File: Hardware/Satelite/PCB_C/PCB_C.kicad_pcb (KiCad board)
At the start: 2 copper layers, 54 x 54 mm, 50 parts, among them IC1 MCP1501T-33E_CHY, IC2 IS25LP080D-JULE-TR, IC3 BQ24392RSER, IC4 MS563702BA03-50, IC5 BMX055, J1 Conn_01x06, J2 JUMPER, J3 Conector_PCB_B-C, J4 Conector_Expansion_CanSat, J5 USB_B_Micro, Q1 BC817, U1 NTB0104BQ,115, U2 TCA9802DGKR, U3 STM32F303RETx, U4 NTB0104BQ,115, U5 SN74LVC1G3157DCKR, U6 Si7006-A20-IM1, Y1 LFXTAL016178, Y2 Crystal

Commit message: PCB C actualizado con nuevo conector (WIP)
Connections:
- J3 pad 1: +BATT -> GND
- J3 pad 10: /I_SENSE_3V3 -> +3V3_Internal
- J3 pad 11: /V_SENSE_3V3 -> /V_SENSE_5V
- J3 pad 12: /V_SENSE_5V -> /I_SENSE_5V
- J3 pad 13: GND -> +5V
- J3 pad 14: +5V -> /5V_ENABLE
- J3 pad 15: GND -> /V_SENSE_3V3
- J3 pad 16: GND -> /I_SENSE_3V3
- J3 pad 17: +3V3_Internal -> +3V3
- J3 pad 18: +3V3 -> /3V_ENABLE
- J3 pad 19: +BATT -> /P1
- J3 pad 2: +BATT -> GND
- J3 pad 20: +BATT -> /GPS_TX
- J3 pad 21: /I_SENSE_BATT -> GND
- J3 pad 22: /GPS_TX -> GND
- J3 pad 23: /P1 -> GND
- J3 pad 24: /SCLK -> /GPOUT
- J3 pad 25: /CS -> /SCL_CHG
- J3 pad 26: /SDI -> /SDA_CHG
- J3 pad 27: /SDO -> VBUS
- J3 pad 28: /S_PARACAIDAS -> /CHG_DISABLE
- J3 pad 29: /S_GLOBO -> /CHG
- J3 pad 3: +3V3 -> GND
- J3 pad 30: /GPOUT -> /ISET
- J3 pad 31: /SDA_CHG -> /I_SENSE_BATT
- J3 pad 32: /SCL_CHG -> /S_GLOBO
- J3 pad 33: /CHG_DISABLE -> /S_PARACAIDAS
- J3 pad 34: /ISET -> /SDO
- J3 pad 35: /CHG -> /SCLK
- J3 pad 36: /3V_ENABLE -> /CS
- J3 pad 37: /5V_ENABLE -> /SDI
- J3 pad 4: GND -> +3V3
- J3 pad 5: GND -> +5V
- J3 pad 6: GND -> +BATT
- J3 pad 7: +5V -> +BATT
- J3 pad 8: GND -> +BATT
- J3 pad 9: /I_SENSE_5V -> +BATT

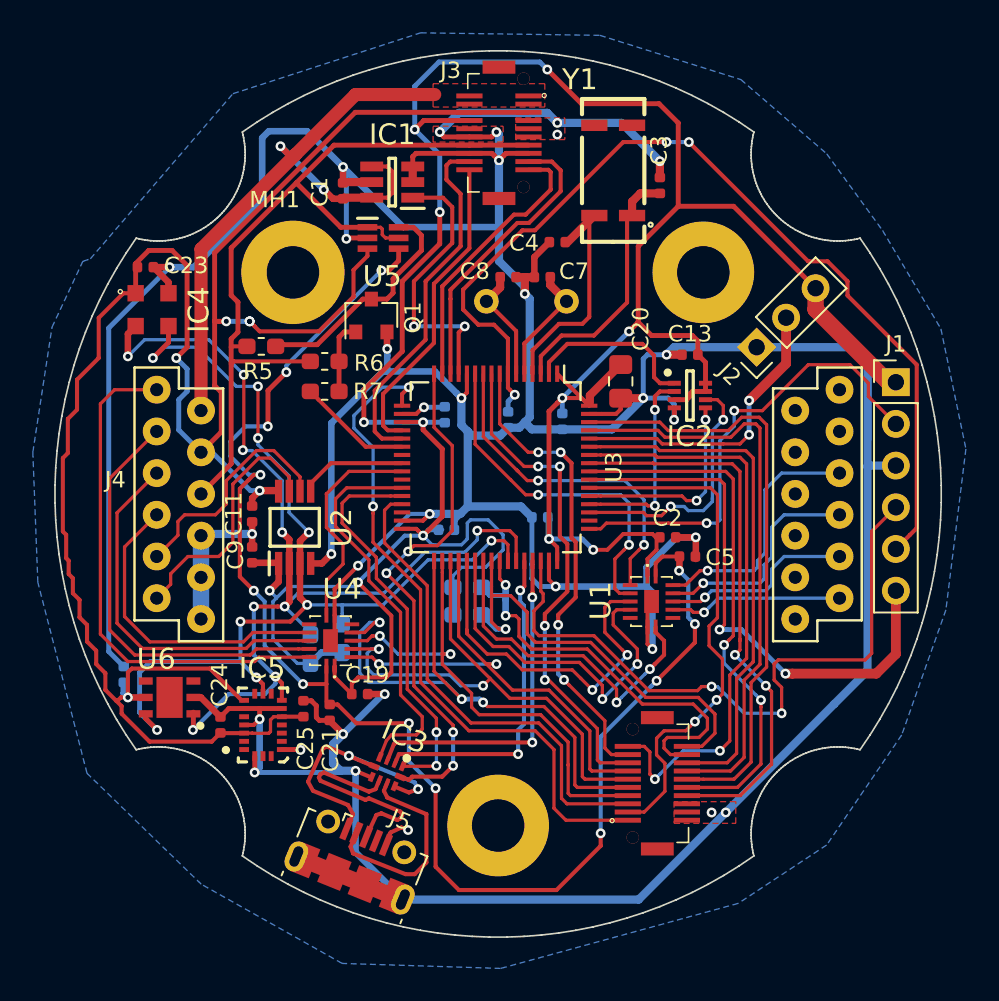
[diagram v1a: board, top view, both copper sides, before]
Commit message: Modificado PCB C para la nueva dispocisión del conector B-C
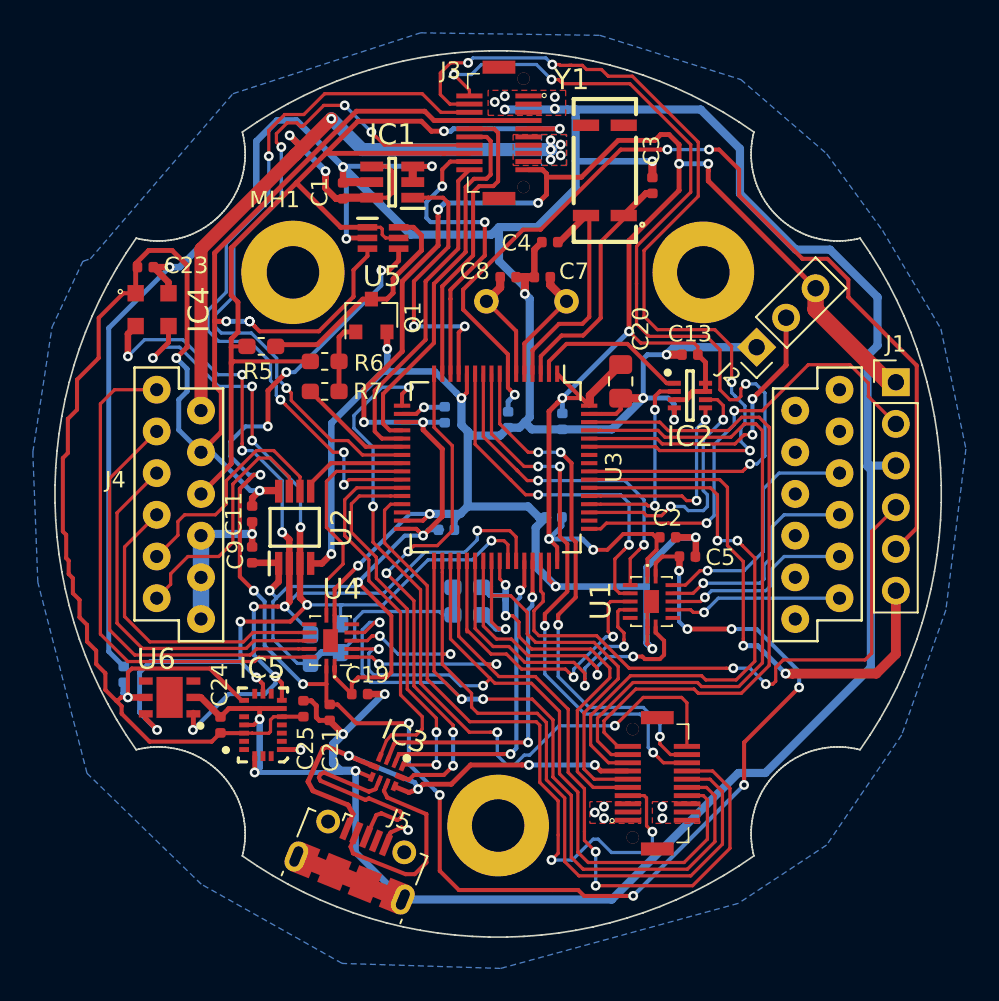
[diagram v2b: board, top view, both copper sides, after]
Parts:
- moved C18 0.86 mm to (3.40, 1.42)
- moved Y1 0.51 mm to (6.50, -19.7)
- moved C3 0.46 mm to (9.40, -18.8)
- moved C4 0.46 mm to (3.15, -15.3)
- moved R3 0.10 mm to (-9.60, 8.79)
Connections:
- U3 pad 23: Net-(U3-Pad23) -> /5V_ENABLE
- U3 pad 26: Net-(U3-Pad26) -> /3V_ENABLE
- U3 pad 29: /P1 -> /GPOUT
- U3 pad 54: /GPS_TX -> /CHG_DISABLE
- U3 pad 56: /3V_ENABLE -> /GPS_TX
- U3 pad 57: /5V_ENABLE -> Net-(U3-Pad57)
- U3 pad 58: /GPOUT -> Net-(U3-Pad58)
- U3 pad 59: /CHG_DISABLE -> /P1
- U3 pad 61: /ISET -> /CHG
- U3 pad 62: /CHG -> /ISET
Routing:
- net /P1: track 29.8 -> 56.7 mm, vias 0 -> 4
- net /GPS_TX: track 32.0 -> 57.7 mm, vias 2 -> 4
- net /SDO: track 29.3 -> 50.0 mm, vias 2 -> 4
- net /SCLK: track 30.3 -> 47.1 mm
- net /CS: track 35.9 -> 51.1 mm
- net /SDI: track 32.1 -> 46.1 mm
- net +3V3_Internal: track 188.1 -> 174.4 mm, vias 12 -> 13
- net +5V: track 50.8 -> 64.4 mm, vias 0 -> 2
- net VBUS: track 16.9 -> 30.4 mm, vias 2 -> 4
- net /3V_ENABLE: track 32.6 -> 45.3 mm, vias 2 -> 4
- net VDD: track 88.5 -> 99.8 mm, vias 12 -> 14
- net GND: track 357.1 -> 367.2 mm, vias 32 -> 36
- net /5V_ENABLE: track 34.3 -> 42.8 mm, vias 2 -> 4
- net +BATT: track 39.7 -> 47.6 mm, vias 2 -> 8
- net /I_SENSE_BATT: track 41.5 -> 47.0 mm, vias 2 -> 4
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- added copper zone on B.Cu, net +BATT
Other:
- net class Default: clearance 0.2 -> 0.18
- rule trace_clearance: 0.2 -> 0.18

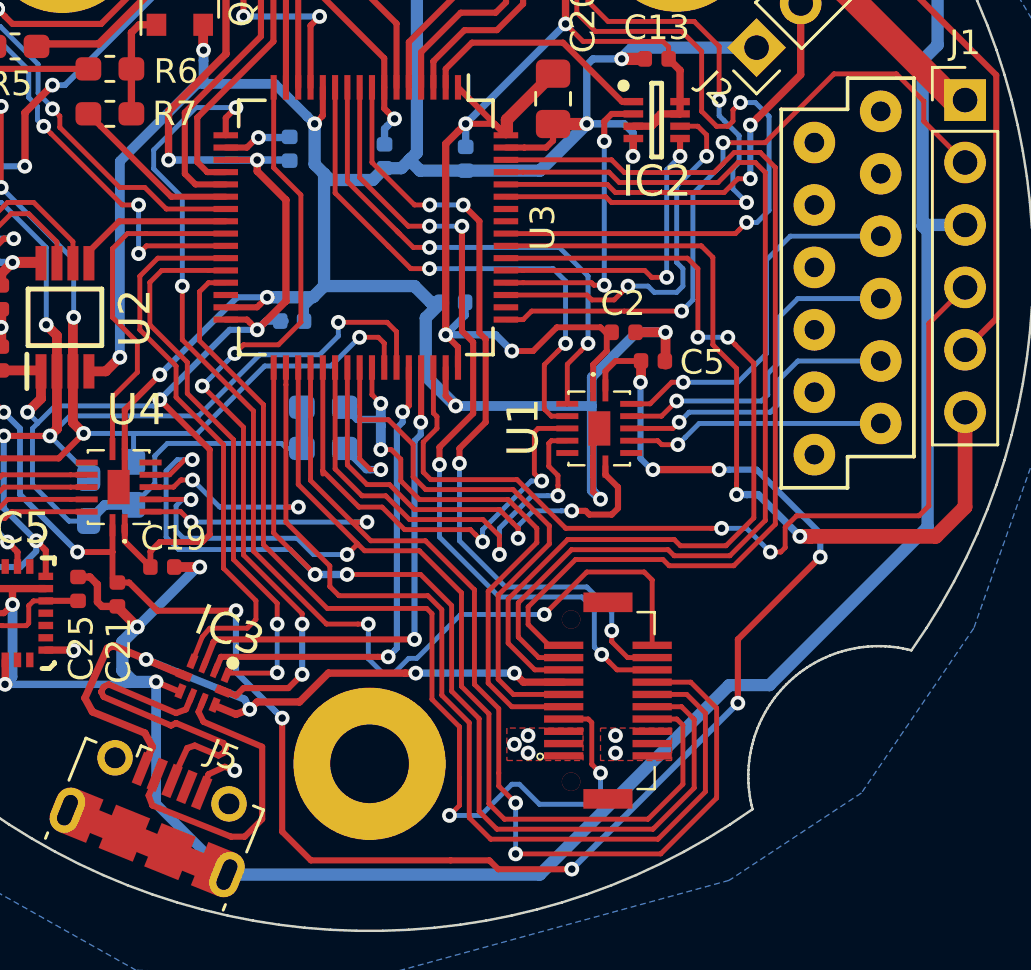
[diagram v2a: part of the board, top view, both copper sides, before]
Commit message: IO3 y IO4 del PCB C al conector de expansión son ahora también UART3 del MCU supervisor
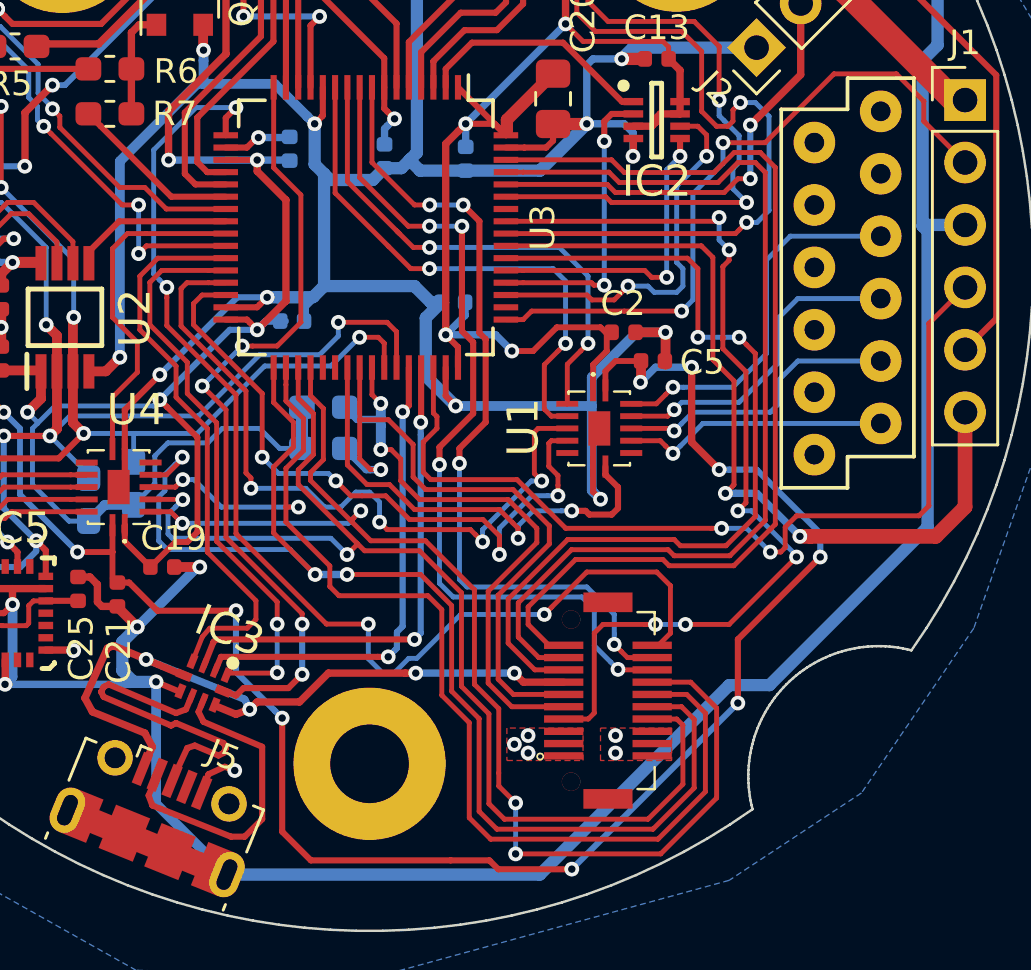
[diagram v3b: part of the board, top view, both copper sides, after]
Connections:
- IC4 pad 2: /SDA -> /Sensor presión/SDA
- U3 pad 29: /GPOUT -> /IO2
- U3 pad 30: Net-(U3-Pad30) -> /IO3
- U3 pad 37: /IO2 -> Net-(U3-Pad37)
- U3 pad 38: /IO3 -> Net-(U3-Pad38)
- U3 pad 57: Net-(U3-Pad57) -> /GPOUT
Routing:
- net /IO2: track 19.3 -> 29.8 mm, vias 2 -> 4
- net /IO3: track 19.8 -> 27.7 mm, vias 2 -> 4
- net /GPOUT: track 40.8 -> 38.9 mm, vias 2 -> 6
- net /S_PARACAIDAS: track 33.8 -> 34.9 mm
- net /I_SENSE_BATT: track 47.0 -> 48.0 mm
- net /S_GLOBO: track 32.5 -> 33.4 mm
- net +3V3_Internal: track 174.4 -> 173.7 mm
- net /SCLK: track 47.1 -> 47.7 mm
- net /SWO: track 33.0 -> 33.6 mm
- net /EXT_IO1: track 13.7 -> 13.2 mm

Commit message: Agregados part number faltantes en PCB_C
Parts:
- added JP1: BOM_Jumper, AXTEC:Empty_Footprint, F.Cu at (20.6, -26.1)
- added M1: Spacer, AXTEC:Empty_Footprint, F.Cu at (24.0, -23.6)
- added M2: Spacer, AXTEC:Empty_Footprint, F.Cu at (23.5, -23.6)
- added M3: Spacer, AXTEC:Empty_Footprint, F.Cu at (23.0, -23.6)
- J2: value JUMPER -> BOOT
- R1, R2, R3, R4: value 10K -> 10k
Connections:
- IC4 pad 2: /Sensor presión/SDA -> /SDA
